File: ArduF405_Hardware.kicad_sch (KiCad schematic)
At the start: 90 parts, among them J1 USB_C_Receptacle_USB2.0, J10 Micro_SD_Card, J3 GPS, J6 ESC, J7 Upper computer connector, Q1 AP40P05, U1 MP9943GQ-Z, U2 RT9013-33GB, U3 RT9013-33GB, U4 STM32F405RGTx, U5 BMI270, U6 AT7456E, U7 W25Q128JVS, U8 SPL06, Y1 YXC 0T252016MJBA4SL, Y2 YXC_XG1EL89CSI-111YLC-27M 27M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

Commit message: 完成原理图绘制
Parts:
- added C19: 10uF(0603 35V 20%), Capacitor_SMD:C_0603_1608Metric, symbol Device:C_Small
- added C20: 1uF(0402 35V 10%), Capacitor_SMD:C_0402_1005Metric, symbol Device:C_Small
- added C21: 100nF(0603 10V 10%), Capacitor_SMD:C_0603_1608Metric, symbol Device:C_Small
- added C22: 100nF(0603 25V 10%), Capacitor_SMD:C_0603_1608Metric, symbol Device:C_Small
- added C44, C45: 22uF(0603 16V), Capacitor_SMD:C_0603_1608Metric, symbol Device:C_Small
- added J12: UART_4, NxtPX4:01x04_MP_sh1.0_Hori, symbol Connector_Generic_MountingPin:Conn_01x04_MountingPin
- added J2: CAM, NxtPX4:01x03_MP_sh1.0_Hori, symbol Connector_Generic_MountingPin:Conn_01x03_MountingPin
- added J4: VTX, symbol Connector_Generic_MountingPin:Conn_01x05_MountingPin
- added J5: DJI O4, NxtPX4:1x06-1MP_P1.00mm_Horizontal, symbol Connector_Generic_MountingPin:Conn_01x06_MountingPin
- added J8: ESC_2, NxtPX4:01x08_MP_sh1.0_Hori, symbol Connector_Generic_MountingPin:Conn_01x08_MountingPin
- added J9: USART_1, NxtPX4:01x04_MP_sh1.0_Hori, symbol Connector_Generic_MountingPin:Conn_01x04_MountingPin
- added L2: 10uH(0420)(78438357100), NxtPX4:Inductor_0420, symbol Device:L_Small
- added R10: 20R(0603 25V), Resistor_SMD:R_0603_1608Metric, symbol Device:R_Small
- added R12: 51kR(0603 25V), Resistor_SMD:R_0603_1608Metric, symbol Device:R_Small
- added R18: 3.6kR(0603 25V), Resistor_SMD:R_0603_1608Metric, symbol Device:R_Small
- added R19: 41.2kR(0603 25V), Resistor_SMD:R_0603_1608Metric, symbol Device:R_Small
- added R35, R36: 10kR(0603), Resistor_SMD:R_0603_1608Metric, symbol Device:R_Small
- added R5: 1MR(0402 50V), Resistor_SMD:R_0402_1005Metric, symbol Device:R_Small
- added R6: 100kR(0603 25V), Resistor_SMD:R_0603_1608Metric, symbol Device:R_Small
- added U19: SN74LVC1G86DCKR, NxtPX4:DCK5, symbol NxtPX4_Symbol:SN74LVC1G86DCKR
- added U9: MP9943GQ-Z, NxtPX4:MP9943GQ-Z, symbol NxtPX4_Symbol:MP9943GQ-Z
- J7: value Upper computer connector -> Upper computer connector/RC input
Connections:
- net BATT_CURRENT_SENS: now also J8.5 (Pin_5)
- net Core_3V3: now also U19.5 (VCC)
- net GND: now also C19.2, C20.2, C21.2, C44.2, C45.2, J12.1 (Pin_1), J12.MP (MountPin), J2.1 (Pin_1), J2.MP (MountPin), J4.2 (Pin_2), J4.MP (MountPin), J5.2 (Pin_2), J5.5 (Pin_5), J8.8 (Pin_8), J8.MP (MountPin), J9.1 (Pin_1), J9.MP (MountPin), R18.1, R35.2, R36.2, U19.3 (GND), U9.5 (GND)
- net System_4V5: now also J12.2 (Pin_2), J2.2 (Pin_2), J9.2 (Pin_2)
- net System_5V: no longer C23.1, C24.1, D7.2 (A), L1.2, R13.2
- net TIM2_CH1: now also J8.4 (Pin_4)
- net TIM2_CH2: now also J8.3 (Pin_3)
- net TIM2_CH3: now also J8.1 (Pin_1)
- net TIM2_CH4: now also J8.2 (Pin_2)
- net TIM9_CH2: now also U19.4; no longer J7.4 (Pin_4)
- net UART4_RX: now also J12.4 (Pin_4), J5.4 (Pin_4)
- net UART4_TX: now also J12.3 (Pin_3), J5.3 (Pin_3)
- net USART1_RX: now also J9.4 (Pin_4)
- net USART1_TX: now also J9.3 (Pin_3)
- net USART3_RX: now also J6.6 (Pin_6)
- net USART6_RX: now also J4.5 (Pin_5)
- net USART6_TX: now also J4.4 (Pin_4)
- net VCC_24V: now also C19.1, C20.1, R5.1, U9.7 (IN)
- net VCC_BAT: now also J8.7 (Pin_7)
- net VIDEO_IN: now also J2.3 (Pin_3)
- net VIDEO_OUT: now also J4.1 (Pin_1)
- net SBUS_INV: now reaches U4.26 (PB0)
- net SBUS_INV: now also R35.1, U19.1
- net LED_0: now reaches U4.46 (PA13)
- net LED_1: now reaches U4.49 (PA14)
- new net: R12.1, U9.1 (FB)
- new net: R12.2, R18.2, R19.1
- new net: R5.2, U9.3 (EN/SYNC)
- new net: C22.1, R10.2
- new net: C22.2, L2.1, U9.6 (SW)
- new net: C21.1, R6.1, U9.2 (VCC)
- new net: R10.1, U9.4 (BST)
- new net: R6.2, U9.8 (PG)
- new net: C23.1, C24.1, D7.2 (A), L1.2, R13.2
- new net CAM_10V: C44.1, C45.1, J4.3 (Pin_3), J5.1 (Pin_1), L2.2, R19.2
- new net SBUS: J5.6 (Pin_6), J7.4 (Pin_4), R36.1, U19.2
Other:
- note added: "10V 3A output"
- note added: "SBUS硬件反相电路"
- moved on the sheet: C17, C2, C23, C24, C3, C30, C37, C4, C41, C7, D7, J10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

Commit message: 完成PCB板设计
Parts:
- added D10, D9: LED_blue, LED_SMD:LED_0603_1608Metric, symbol Device:LED
- added D8: LED_Red, LED_SMD:LED_0603_1608Metric, symbol Device:LED
- added R20, R21, R22: 3.6kR(0603 25V), Resistor_SMD:R_0603_1608Metric, symbol Device:R_Small
- H1, H2, H3, H4: footprint MountingHole:MountingHole_3mm_Pad -> MountingHole:MountingHole_4.3mm_M4_DIN965_Pad
- J4: footprint (none) -> NxtPX4:01x05_MP_sh1.0_Hori
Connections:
- net GNDD is gone; now on net GND: H1.1, H2.1, H3.1, H4.1
- net Core_3V3: now also D8.2 (A)
- net GND: now also J5.MP (MountPin), R20.1, R21.1, R22.1
- net LED_0: now also D9.2 (A)
- net LED_1: now also D10.2 (A)
- net USART3_RX: now also J8.6 (Pin_6)
- new net: D10.1 (K), R22.2
- new net: D9.1 (K), R21.2
- new net: D8.1 (K), R20.2
- no-connect marks 17 -> 16
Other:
- note added: "LED指示灯"
- note added: "blue(ACT)"
- note added: "green(B/E)"
- note added: "red(3v3 Indicator)"

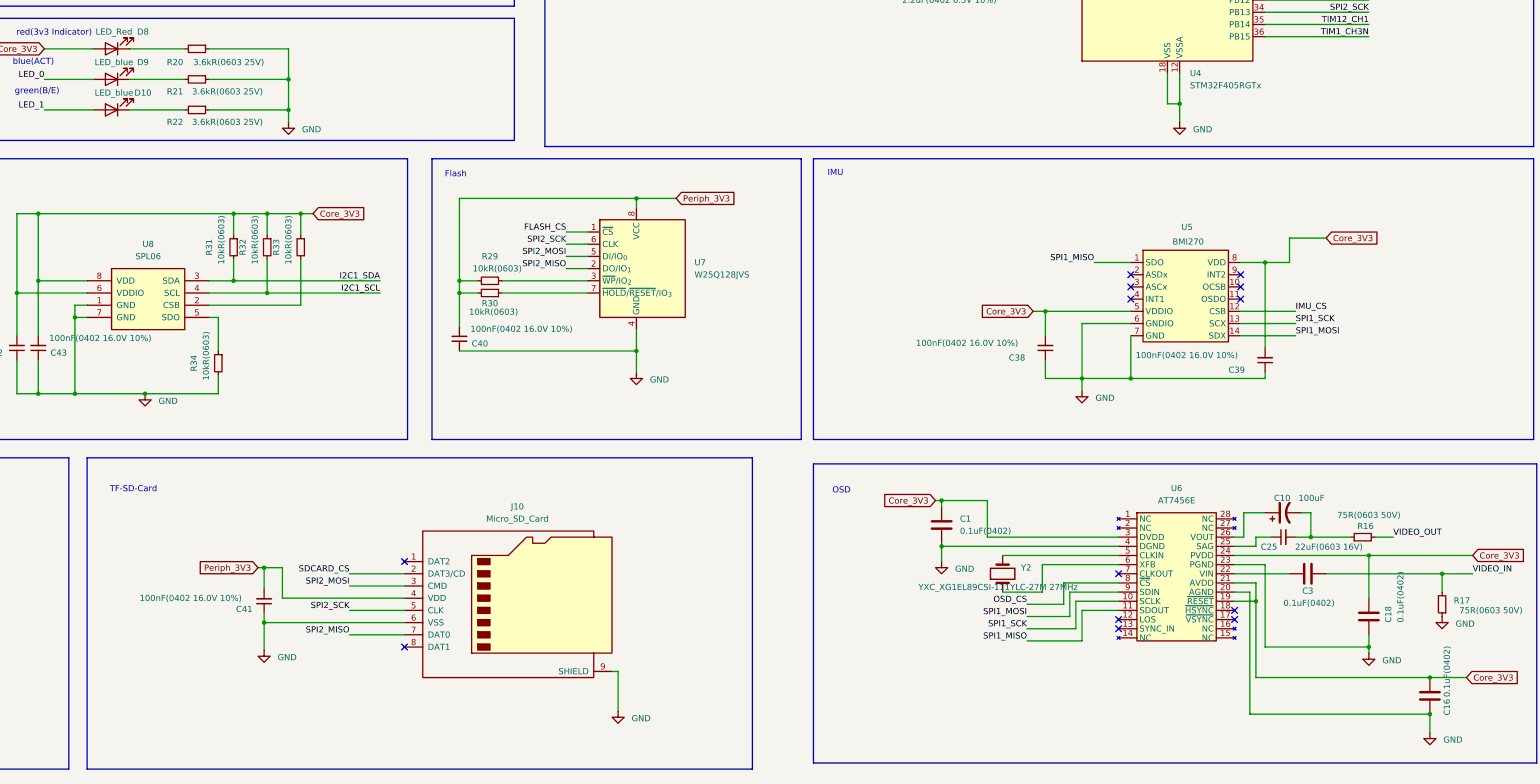
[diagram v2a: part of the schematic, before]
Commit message: 细节修改，led表示错误修正
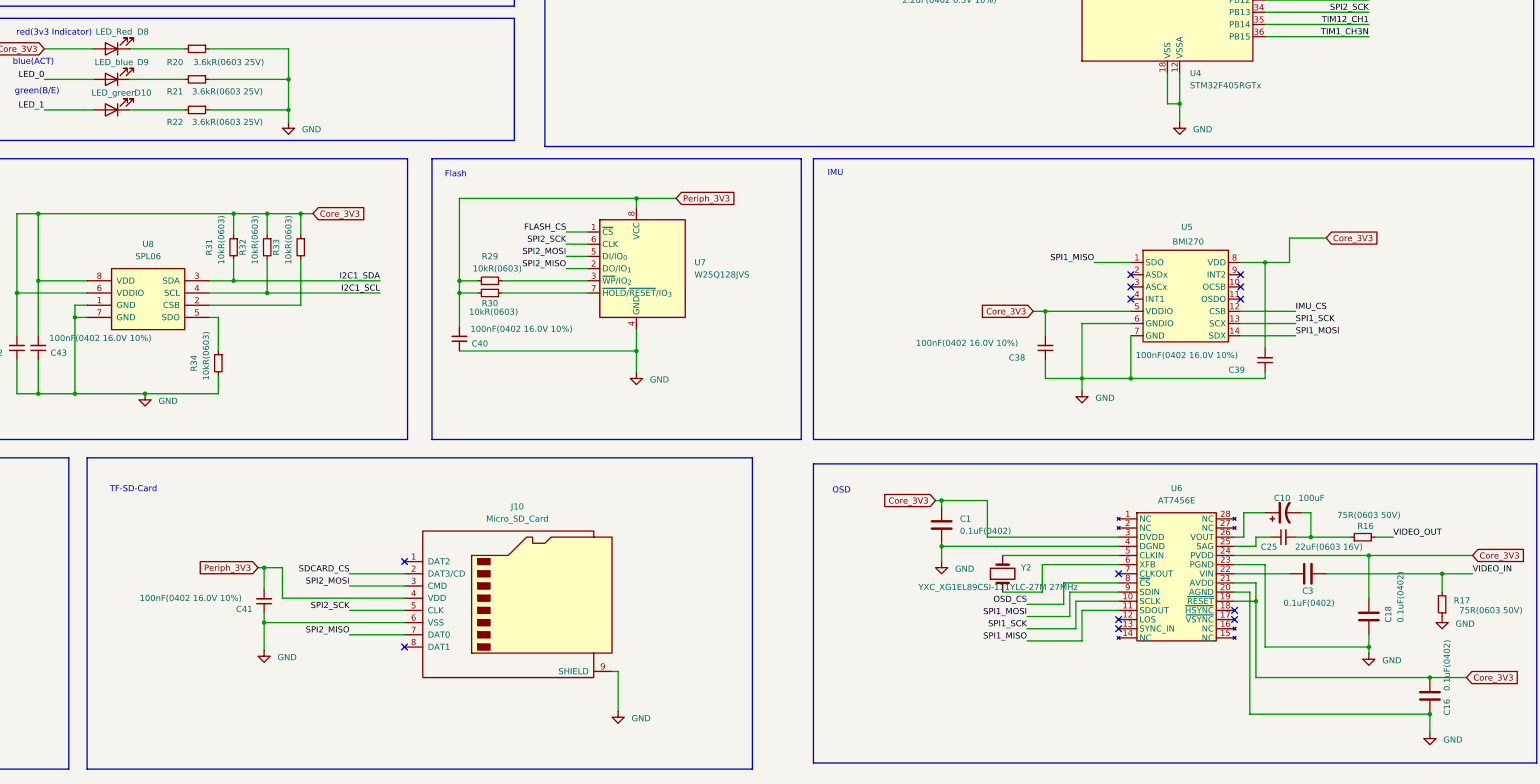
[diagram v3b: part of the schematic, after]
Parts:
- D10: value LED_blue -> LED_green
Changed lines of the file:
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@@
 		)
 		(property "Value" "0.1uF(0402)"
-			(at 558.546 289.814 90)
+			(at 558.546 288.544 90)
 			(show_name no)
 			(do_not_autoplace no)
@@
 			)
 		)
-		(property "Value" "LED_blue"
+		(property "Value" "LED_green"
 			(at 281.178 164.084 0)
 			(show_name no)
